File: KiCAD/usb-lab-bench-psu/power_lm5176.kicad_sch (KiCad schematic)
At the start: 50 parts, among them J10 Conn_01x03, Q5 NMOS, Q6 DMN6040SK3, Q7 DMN6040SK3, Q8 DMN6040SK3, Q9 DMN6040SK3, U10 MCP4725xxx-xCH, U9 LM5176PWP

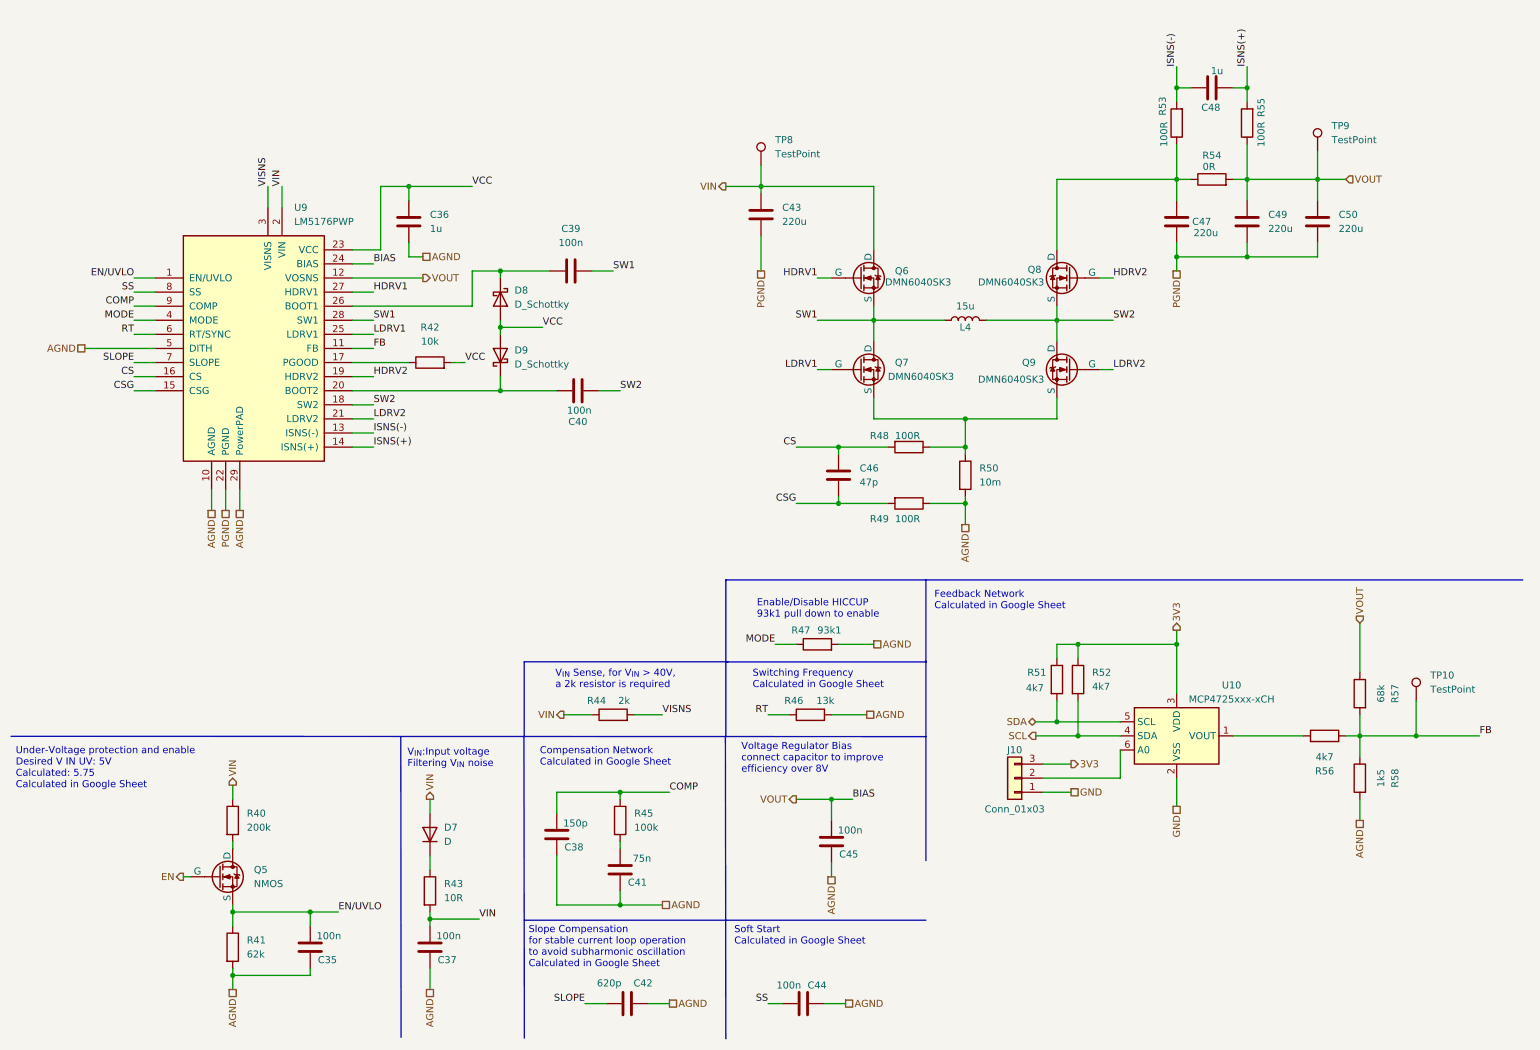
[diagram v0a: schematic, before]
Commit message: Updated schematic for buck-boost-converter
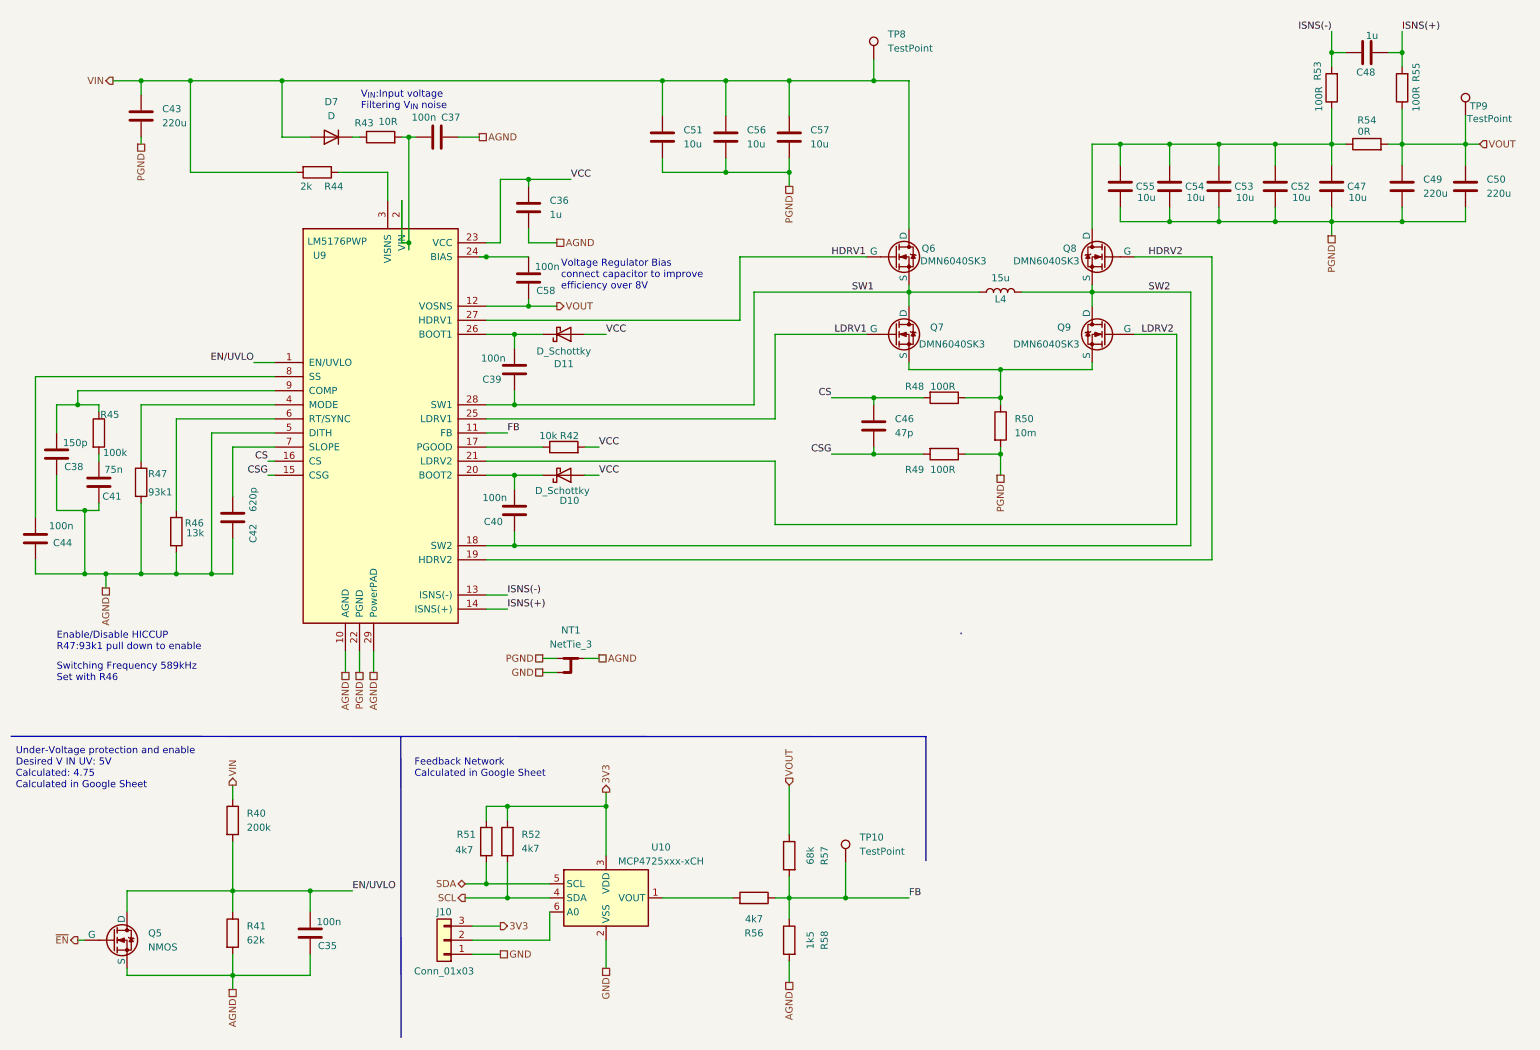
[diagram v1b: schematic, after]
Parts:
- removed C45: 100n, symbol Device:C
- removed D8, D9: D_Schottky, symbol Device:D_Schottky
- added C51, C52, C53, C54, C55, C56, C57: 10u, symbol Device:C
- added C58: 100n, symbol Device:C
- added D10, D11: D_Schottky, symbol Device:D_Schottky
- added NT1: NetTie_3, symbol Device:NetTie_3
- C47: value 220u -> 10u
- U9: symbol Regulator_Switching:LM5176PWP -> Prj_dcdc_converter:LM5176PWPR
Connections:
- net AGND: now also C36.1, Q5.3 (S), NT1.2; no longer C36.2, R49.1, R50.2
- net EN/UVLO: now also Q5.1 (D), R40.2; no longer Q5.3 (S)
- net GND: now also NT1.3
- net PGND: now also R49.1, R50.2, C51.2, C52.2, C53.2, C54.2, C55.2, C56.2, C57.2, NT1.1
- net SW2: now also C40.1; no longer C40.2
- net VCC: now also C36.2, D10.2 (A), D11.2 (A); no longer C36.1
- net VIN: now also R44.2, C51.1, C56.1, C57.1; no longer C37.1, R43.2, R44.1, U9.2 (VIN)
- net VOUT: now also C58.2; no longer U9.24 (BIAS)
- net at U9.20 (BOOT2): now also C40.2, D10.1 (K); no longer C40.1
- net at C39.1, U9.26 (BOOT1): now also D11.1 (K)
- net at C47.1, Q8.1 (D), R53.1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: now also C52.1, C53.1, C54.1, C55.1
- net COMP: no longer names the net of C38.1, R45.1, U9.9 (COMP)
- net EN renamed ~{EN}
- net MODE: no longer names the net of R47.1, U9.4 (MODE)
- net RT: no longer names the net of R46.1, U9.6 (RT/SYNC)
- net SLOPE: no longer names the net of C42.1, U9.7 (SLOPE)
- net SS: no longer names the net of C44.1, U9.8 (SS)
- net VISNS: no longer names the net of U9.3 (VISNS)
- net VISNS: now also R44.1; no longer R44.2
- new net: C37.1, R43.2, U9.2 (VIN)
- new net: C58.1, U9.24 (BIAS)
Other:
- note added: "Enable/Disable HICCUP R47:93k1 pull down to enable"
- note added: "Switching Frequency 589kHz Set with R46"
- note added: "Under-Voltage protection and enable Desired V IN UV: 5V Calculated: 4.75 Calculated in Google Sheet"
- note removed: "Compensation Network Calculated in Google Sheet"
- note removed: "Enable/Disable HICCUP 93k1 pull down to enable"
- note removed: "Slope Compensation for stable current loop operation to avoid subharmonic oscillation Calculated in Google Sheet"
- note removed: "Soft Start Calculated in Google Sheet"
- note removed: "Switching Frequency Calculated in Google Sheet"
- note removed: "Under-Voltage protection and enable Desired V IN UV: 5V Calculated: 5.75 Calculated in Google Sheet"
- note removed: "V_{IN} Sense, for V_{IN} > 40V, a 2k resistor is required"
- moved on the sheet: C35, C36, C38, C39, C40, C41, C42, C44, C46, C47, C48, C49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

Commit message: added current limitting feedback circuit
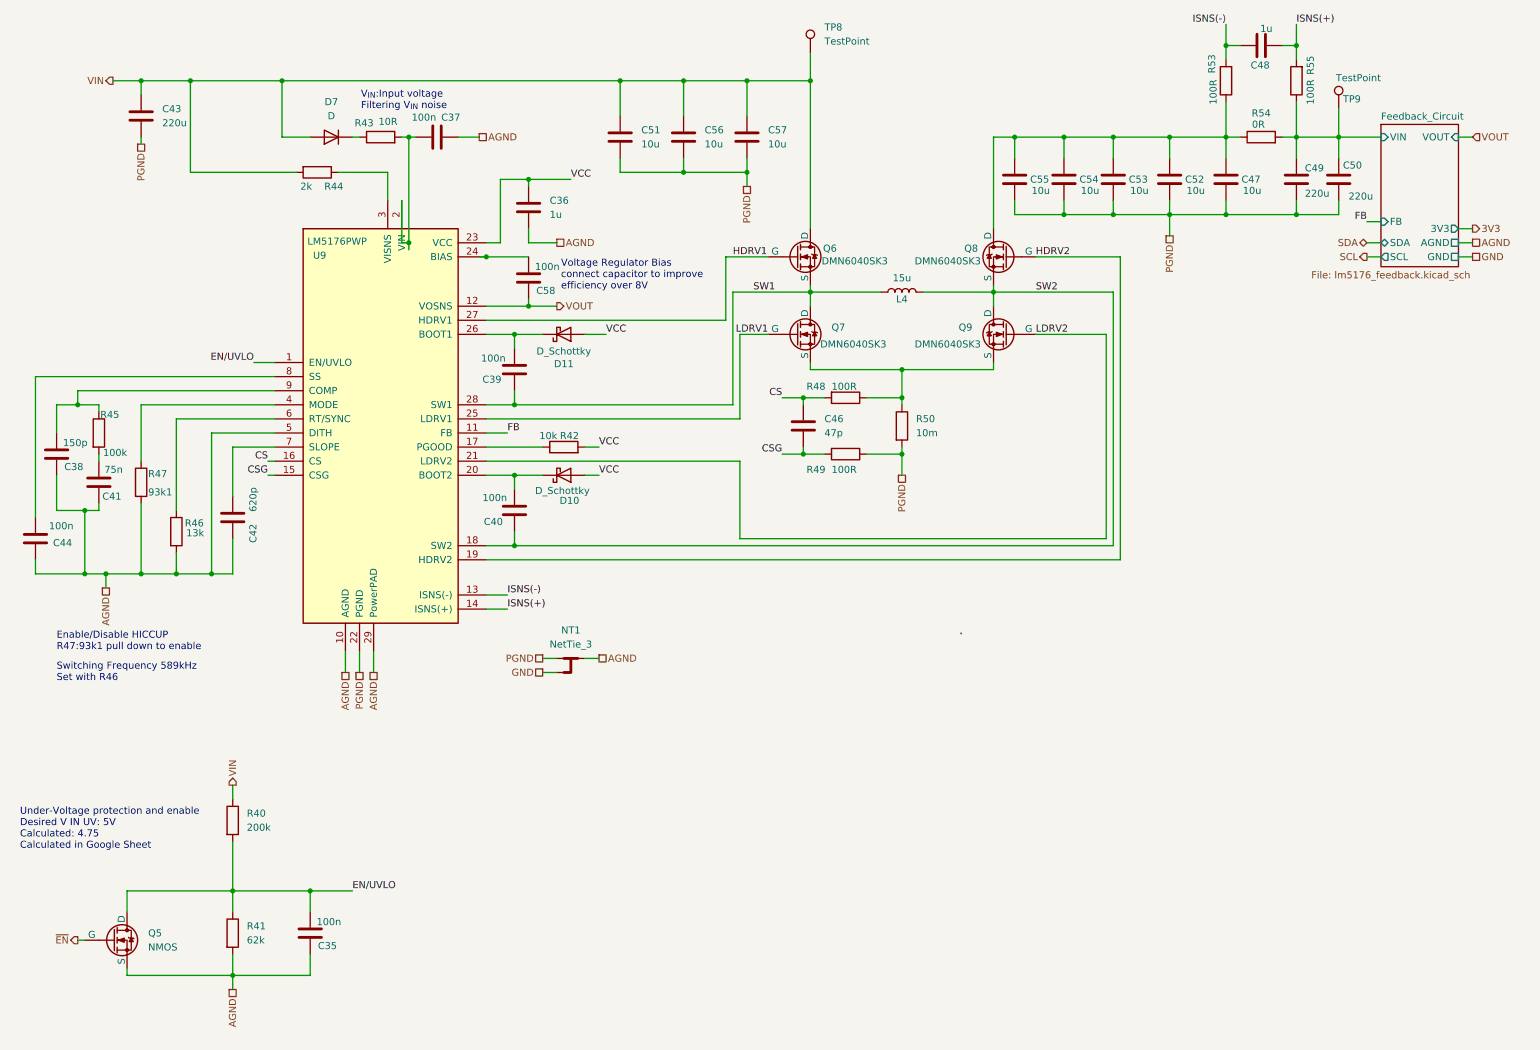
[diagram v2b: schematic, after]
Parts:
- removed J10: Conn_01x03, symbol Connector_Generic:Conn_01x03
- removed R51, R52, R56: 4k7, symbol Device:R
- removed R57: 68k, symbol Device:R
- removed R58: 1k5, symbol Device:R
- removed TP10: TestPoint, symbol Connector:TestPoint
- removed U10: MCP4725xxx-xCH, Package_TO_SOT_SMD:SOT-23-6, symbol Analog_DAC:MCP4725xxx-xCH
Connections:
- net VOUT: no longer C49.1, C50.1, R54.2, R55.1, TP9.1
- new net Feedback_Circuit/VIN: C49.1, C50.1, R54.2, R55.1, TP9.1
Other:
- added sheet Feedback_Circuit (lm5176_feedback.kicad_sch)
- note removed: "Feedback Network Calculated in Google Sheet"
- moved on the sheet: C46, C47, C48, C49, C50, C51, C52, C53, C54, C55, C56, C57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

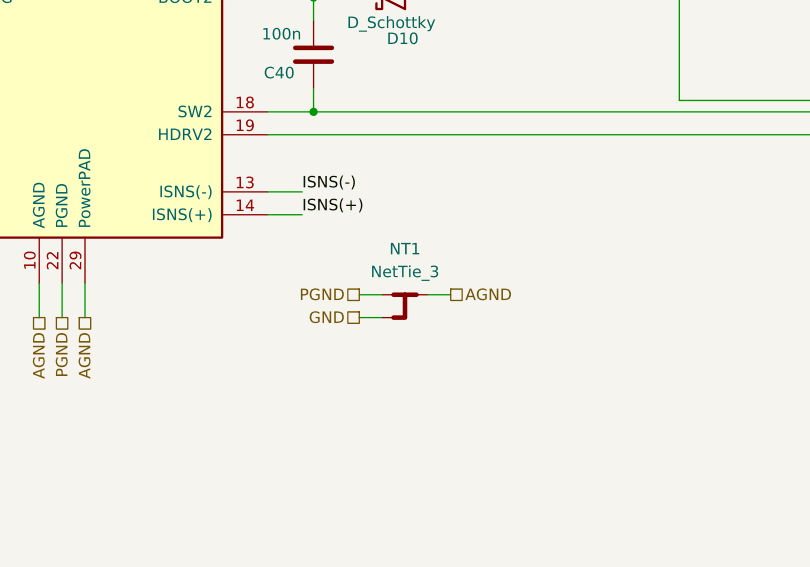
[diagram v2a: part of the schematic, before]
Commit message: restructured schematics to better show individual boards
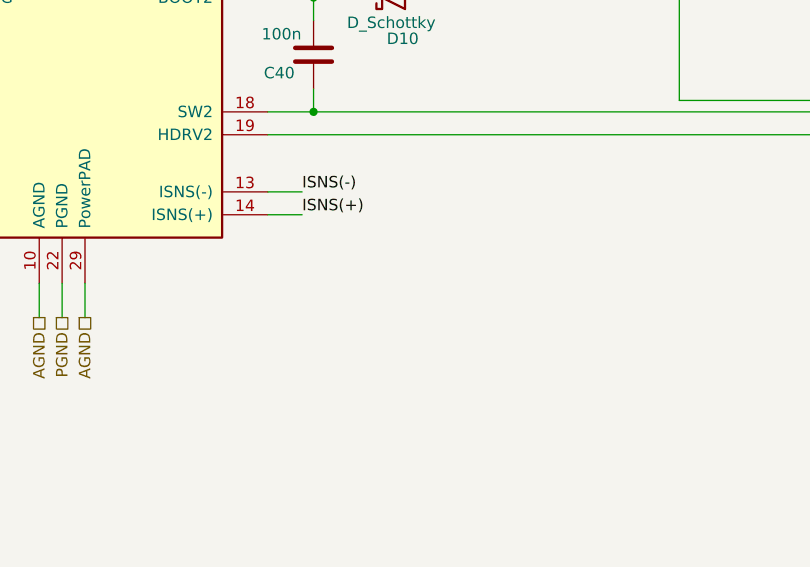
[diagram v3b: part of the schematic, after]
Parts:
- removed NT1: NetTie_3, symbol Device:NetTie_3

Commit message: updated spi for display
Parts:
- renumbered C44 to C68, C38 to C69, C41 to C70, C43 to C71, C42 to C72, C35 to C73, C37 to C74, C39 to C75, C40 to C76, C36 to C77, C58 to C78, C51 to C79, C56 to C80, C57 to C81, C46 to C82, C55 to C83, C54 to C84, C53 to C85, C52 to C86, C47 to C87, C48 to C88, C49 to C89, C50 to C90, D7 to D14, D11 to D15, D10 to D16, L4 to L8, Q7 to Q10, Q8 to Q11, Q9 to Q12, Q5 to Q3, Q6 to Q4, R45 to R77, R47 to R78, R46 to R79, R40 to R80, R41 to R81, R44 to R82, R43 to R83, R42 to R84, R48 to R85, R49 to R86, R50 to R87, R53 to R88, R54 to R89, R55 to R90, TP8 to TP14, TP9 to TP15, U9 to U15
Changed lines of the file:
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@@
 		(on_board yes)
 		(dnp no)
-		(property "Reference" "C41"
+		(property "Reference" "C70"
 			(at 32.004 100.33 0)
 			(effects
@@
 		(on_board yes)
 		(dnp no)
-		(property "Reference" "C50"
+		(property "Reference" "C90"
 			(at 252.222 40.64 0)
 			(effects
@@
 		(on_board yes)
 		(dnp no)
-		(property "Reference" "R44"
+		(property "Reference" "R82"
 			(at 68.5801 44.45 90)
 			(effects
@@
 		(on_board yes)
 		(dnp no)
-		(property "Reference" "L4"
+		(property "Reference" "L8"
 			(at 172.72 64.77 90)
 			(effects
@@
 		(dnp no)
 		(fields_autoplaced yes)
-		(property "Reference" "C43"
+		(property "Reference" "C71"
 			(at 39.37 30.4799 0)
 			(effects
@@
 		(on_board yes)
 		(dnp no)
-		(property "Reference" "C49"
+		(property "Reference" "C89"
 			(at 245.364 41.148 0)
 			(effects
@@
 		(on_board yes)
 		(dnp no)
-		(property "Reference" "R48"
+		(property "Reference" "R85"
 			(at 157.226 80.518 90)
 			(effects
@@
 		(on_board yes)
 		(dnp no)
-		(property "Reference" "C40"
+		(property "Reference" "C76"
 			(at 99.06 104.902 0)
 			(effects
@@
 		(dnp no)
 		(fields_autoplaced yes)
-		(property "Reference" "C56"
+		(property "Reference" "C80"
 			(at 137.16 34.2899 0)
 			(effects
@@
 		(on_board yes)
 		(dnp no)
-		(property "Reference" "C39"
+		(property "Reference" "C75"
 			(at 98.806 79.248 0)
 			(effects
@@
 		(on_board yes)
 		(dnp no)
-		(property "Reference" "Q6"
+		(property "Reference" "Q4"
 			(at 158.496 55.626 0)
 			(effects
@@
 		(dnp no)
 		(fields_autoplaced yes)
-		(property "Reference" "C57"
+		(property "Reference" "C81"
 			(at 148.59 34.2899 0)
 			(effects
@@
 		(on_board yes)
 		(dnp no)
-		(property "Reference" "R43"
+		(property "Reference" "R83"
 			(at 77.4699 33.02 90)
 			(effects
@@
 		(on_board yes)
 		(dnp no)
-		(property "Reference" "Q9"
+		(property "Reference" "Q12"
 			(at 185.42 69.8499 0)
 			(effects
@@
 		(dnp no)
 		(fields_autoplaced yes)
-		(property "Reference" "TP8"
+		(property "Reference" "TP14"
 			(at 158.75 15.7479 0)
 			(effects
@@
 		(on_board yes)
 		(dnp no)
-		(property "Reference" "R55"
+		(property "Reference" "R90"
 			(at 246.38 22.606 90)
 			(effects
@@
 		(on_board yes)
 		(dnp no)
-		(property "Reference" "TP9"
+		(property "Reference" "TP15"
 			(at 252.222 28.702 0)
 			(effects
@@
 		(dnp no)
 		(fields_autoplaced yes)
-		(property "Reference" "R41"
+		(property "Reference" "R81"
 			(at 54.61 177.7999 0)
 			(effects
@@
 		(on_board yes)
 		(dnp no)
-		(property "Reference" "C44"
+		(property "Reference" "C68"
 			(at 23.114 108.712 0)
 			(effects
@@
 		(on_board yes)
 		(dnp no)
-		(property "Reference" "R54"
+		(property "Reference" "R89"
 			(at 237.49 31.242 90)
 			(effects
@@
 		(on_board yes)
 		(dnp no)
-		(property "Reference" "R49"
+		(property "Reference" "R86"
 			(at 157.226 95.504 90)
 			(effects
@@
 		(on_board yes)
 		(dnp no)
-		(property "Reference" "R46"
+		(property "Reference" "R79"
 			(at 43.434 105.156 0)
 			(effects
@@
 		(on_board yes)
 		(dnp no)
-		(property "Reference" "R45"
+		(property "Reference" "R77"
 			(at 28.194 85.598 0)
 			(effects
@@
 		(on_board yes)
 		(dnp no)
-		(property "Reference" "Q7"
+		(property "Reference" "Q10"
 			(at 160.02 69.8499 0)
 			(effects
@@
 		(on_board yes)
 		(dnp no)
-		(property "Reference" "C37"
+		(property "Reference" "C74"
 			(at 89.662 32.004 90)
 			(effects
@@
 		(dnp no)
 		(fields_autoplaced yes)
-		(property "Reference" "C51"
+		(property "Reference" "C79"
 			(at 125.73 34.2899 0)
 			(effects
@@
 		(on_board yes)
 		(dnp no)
-		(property "Reference" "R42"
+		(property "Reference" "R84"
 			(at 112.776 89.408 90)
 			(effects
@@
 		(dnp no)
 		(fields_autoplaced yes)
-		(property "Reference" "C36"
+		(property "Reference" "C77"
 			(at 109.22 46.9899 0)
 			(effects
@@
 		(on_board yes)
 		(dnp no)
-		(property "Reference" "C53"
+		(property "Reference" "C85"
 			(at 213.614 43.18 0)
 			(effects
@@
 		(on_board yes)
 		(dnp no)
-		(property "Reference" "U9"
+		(property "Reference" "U15"
 			(at 66.548 56.896 0)
 			(effects
@@
 		(on_board yes)
 		(dnp no)
-		(property "Reference" "C52"
+		(property "Reference" "C86"
 			(at 223.774 43.18 0)
 			(effects
@@
 		(dnp no)
 		(fields_autoplaced yes)
-		(property "Reference" "R50"
+		(property "Reference" "R87"
 			(at 175.26 86.3599 0)
 			(effects
@@
 		(on_board yes)
 		(dnp no)
-		(property "Reference" "C58"
+		(property "Reference" "C78"
 			(at 110.236 63.246 0)
 			(effects
@@
 		(on_board yes)
 		(dnp no)
-		(property "Reference" "C48"
+		(property "Reference" "C88"
 			(at 239.014 22.606 90)
 			(effects
@@
 		(on_board yes)
 		(dnp no)
-		(property "Reference" "C55"
+		(property "Reference" "C83"
 			(at 195.834 43.18 0)
 			(effects
@@
 		(on_board yes)
 		(dnp no)
-		(property "Reference" "R47"
+		(property "Reference" "R78"
 			(at 36.83 96.266 0)
 			(effects
@@
 		(on_board yes)
 		(dnp no)
-		(property "Reference" "D10"
+		(property "Reference" "D16"
 			(at 112.776 101.092 0)
 			(effects
@@
 		(dnp no)
 		(fields_autoplaced yes)
-		(property "Reference" "D7"
+		(property "Reference" "D14"
 			(at 69.85 29.21 0)
 			(effects
@@
 		(dnp no)
 		(fields_autoplaced yes)
-		(property "Reference" "Q5"
+		(property "Reference" "Q3"
 			(at 36.83 179.0699 0)
 			(effects
@@
 		(on_board yes)
 		(dnp no)
-		(property "Reference" "C35"
+		(property "Reference" "C73"
 			(at 70.866 181.356 0)
 			(effects
@@
 		(dnp no)
 		(fields_autoplaced yes)
-		(property "Reference" "C46"
+		(property "Reference" "C82"
 			(at 158.75 86.3599 0)
 			(effects
@@
 		(on_board yes)
 		(dnp no)
-		(property "Reference" "C38"
+		(property "Reference" "C69"
 			(at 25.146 94.996 0)
 			(effects
@@
 		(on_board yes)
 		(dnp no)
-		(property "Reference" "C54"
+		(property "Reference" "C84"
 			(at 204.724 43.18 0)
 			(effects
@@
 		(on_board yes)
 		(dnp no)
-		(property "Reference" "Q8"
+		(property "Reference" "Q11"
 			(at 186.436 55.626 0)
 			(effects
@@
 		(on_board yes)
 		(dnp no)
-		(property "Reference" "D11"
+		(property "Reference" "D15"
 			(at 111.76 76.454 0)
 			(effects
@@
 		(dnp no)
 		(fields_autoplaced yes)
-		(property "Reference" "R40"
+		(property "Reference" "R80"
 			(at 54.61 157.4799 0)
 			(effects
@@
 		(on_board yes)
 		(dnp no)
-		(property "Reference" "C42"
+		(property "Reference" "C72"
 			(at 55.753 105.283 90)
 			(effects
@@
 		(on_board yes)
 		(dnp no)
-		(property "Reference" "R53"
+		(property "Reference" "R88"
 			(at 228.6 22.352 90)
 			(effects
@@
 		(on_board yes)
 		(dnp no)
-		(property "Reference" "C47"
+		(property "Reference" "C87"
 			(at 233.934 43.18 0)
 			(effects

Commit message: added current limiting circuit for USB PD sink, added 2nd buck converter
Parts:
- C54: renamed from C71; symbol Device:C -> Device:C_Polarized
- C72: renamed from C89; symbol Device:C -> Device:C_Polarized
- C73: renamed from C90; symbol Device:C -> Device:C_Polarized
- renumbered C68 to C51, C69 to C52, C70 to C53, C72 to C55, C73 to C56, C74 to C57, C75 to C58, C76 to C59, C77 to C60, C78 to C61, C79 to C62, C80 to C63, C81 to C64, C82 to C65, C83 to C66, C84 to C67, C85 to C68, C86 to C69, C87 to C70, C88 to C71, D14 to D11, D15 to D12, D16 to D13, L8 to L7, Q3 to Q4, Q4 to Q5, Q10 to Q6, Q11 to Q7, Q12 to Q8, R77 to R64, R78 to R65, R79 to R66, R80 to R67, R81 to R68, R82 to R69, R83 to R70, R84 to R71, R85 to R72, R86 to R73, R87 to R74, R88 to R75, R89 to R76, R90 to R77, TP14 to TP13, TP15 to TP14, U15 to U17
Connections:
- net Feedback_Circuit/VIN is gone; now on net VOUT: C72.1, C73.1, R76.2, R77.1, TP14.1
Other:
- removed sheet Feedback_Circuit
- moved on the sheet: D11, R70
